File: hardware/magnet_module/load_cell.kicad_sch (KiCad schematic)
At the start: 18 parts, among them J7 691137710004, U4 NAU7802, U5 KC2520Z4.91520C1KX00

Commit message: Make Alogus-requested mechanical changes
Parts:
- J7: value 691137710004 -> S4B-XH-A-1(LF)(SN); footprint TerminalBlock_RND:TerminalBlock_RND_205-00003_1x04_P5.00mm_Horizontal -> Connector_JST:JST_XH_S4B-XH-A-1_1x04_P2.50mm_Horizontal; LCSC C7032066 -> C163037; MPN 691137710004 -> S4B-XH-A-1(LF)(SN)
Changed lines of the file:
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@@
 			)
 		)
-		(property "Value" "691137710004"
+		(property "Value" "S4B-XH-A-1(LF)(SN)"
 			(at 47.752 64.77 0)
 			(effects
@@
 			)
 		)
-		(property "Footprint" "TerminalBlock_RND:TerminalBlock_RND_205-00003_1x04_P5.00mm_Horizontal"
+		(property "Footprint" "Connector_JST:JST_XH_S4B-XH-A-1_1x04_P2.50mm_Horizontal"
 			(at 46.99 71.12 0)
 			(effects
@@
 			)
 		)
-		(property "MPN" "691137710004"
+		(property "MPN" "S4B-XH-A-1(LF)(SN)"
 			(at 46.99 71.12 0)
 			(effects
@@
 			)
 		)
-		(property "LCSC" "C7032066"
+		(property "LCSC" "C163037"
 			(at 46.99 71.12 0)
 			(effects

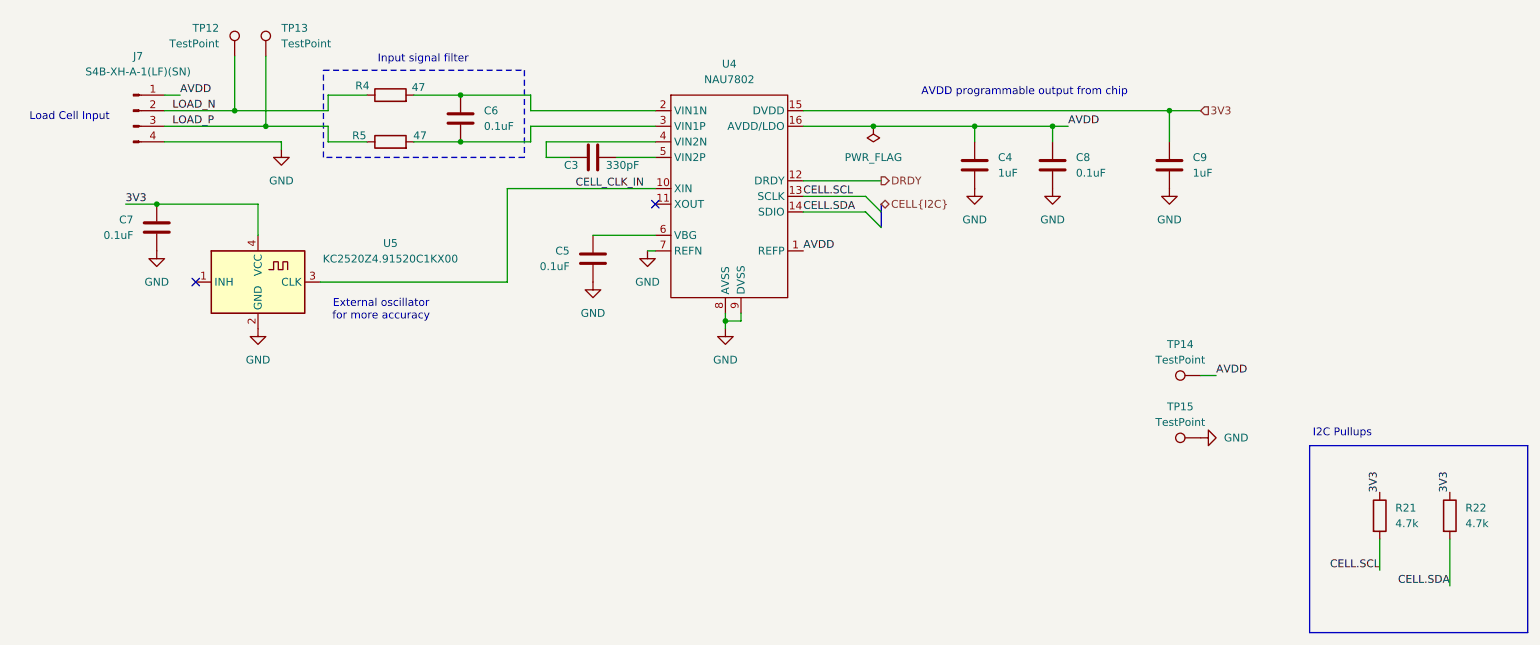
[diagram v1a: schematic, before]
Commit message: add test points to schematic, generate step file including ultrasonic mic
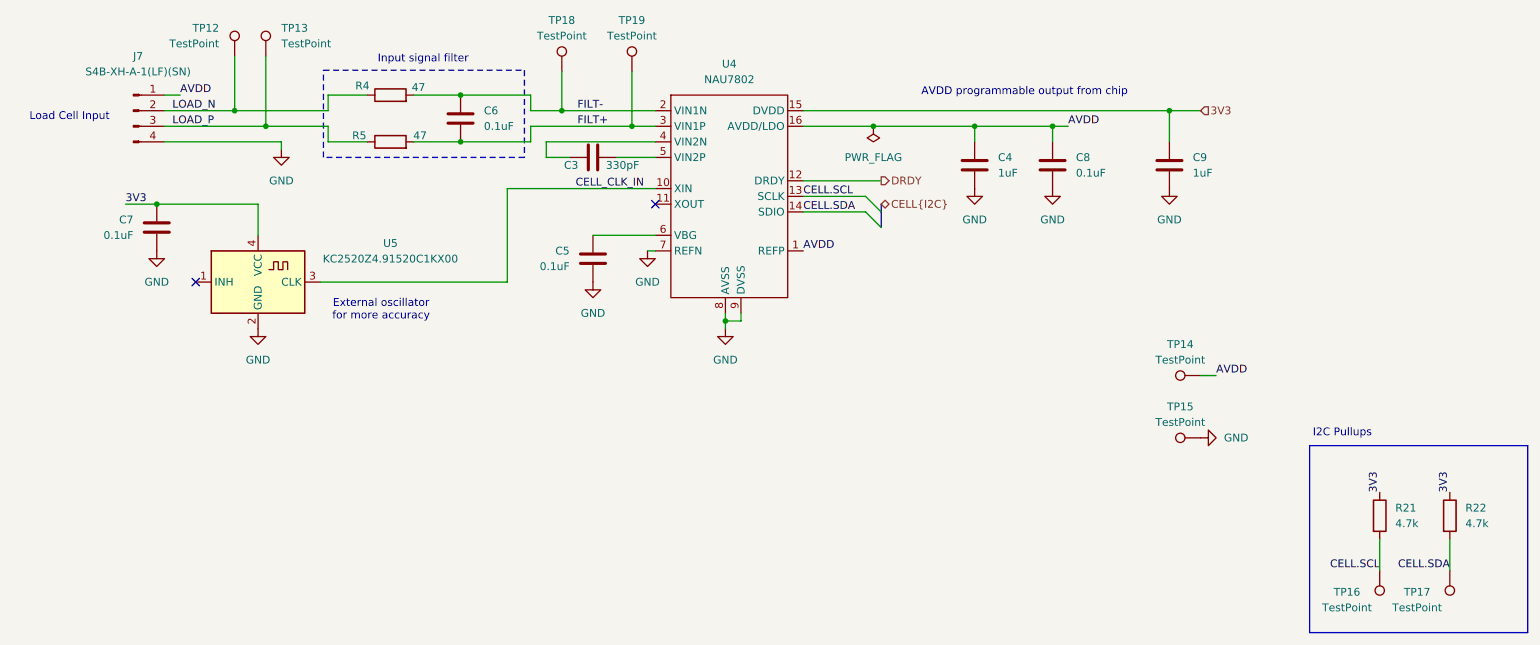
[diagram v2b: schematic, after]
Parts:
- added TP16, TP17, TP18, TP19: TestPoint, TestPoint:TestPoint_Pad_1.0x1.0mm, symbol Connector:TestPoint
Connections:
- net CELL.SCL: now also TP16.1
- net CELL.SDA: now also TP17.1
- net FILT-: now reaches C6.1, R4.2, U4.2 (VIN1N)
- net FILT-: now also TP18.1
- net FILT+: now reaches C6.2, R5.2, U4.3 (VIN1P)
- net FILT+: now also TP19.1
